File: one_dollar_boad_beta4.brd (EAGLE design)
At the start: 85.6 x 54 mm, 38 parts, among them IC1 ATTINY85, X1 USBPCB

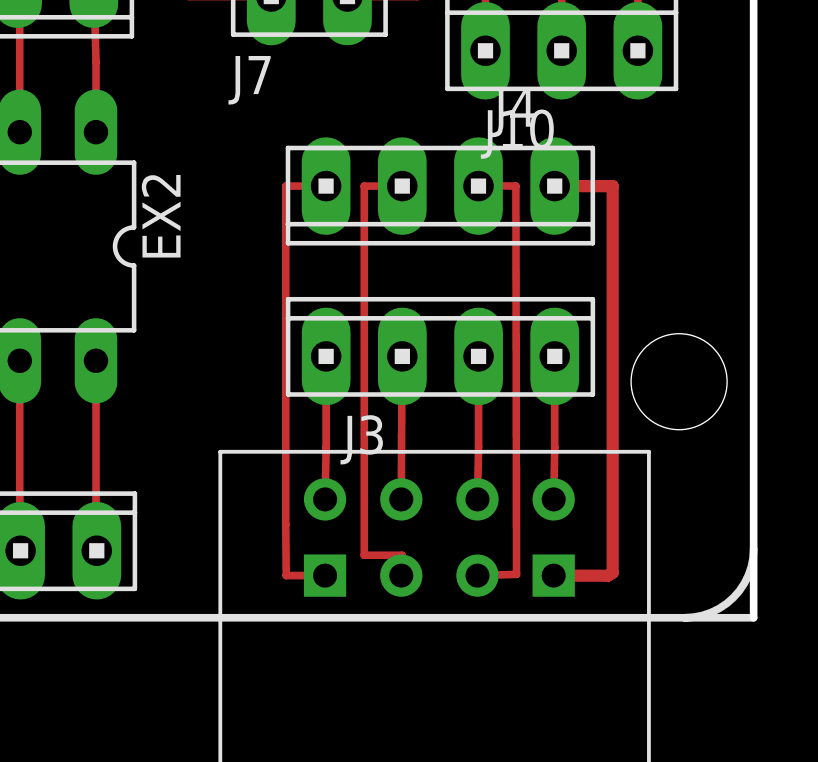
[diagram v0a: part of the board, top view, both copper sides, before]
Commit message: aumentada espessura das trilhas do ESP8266
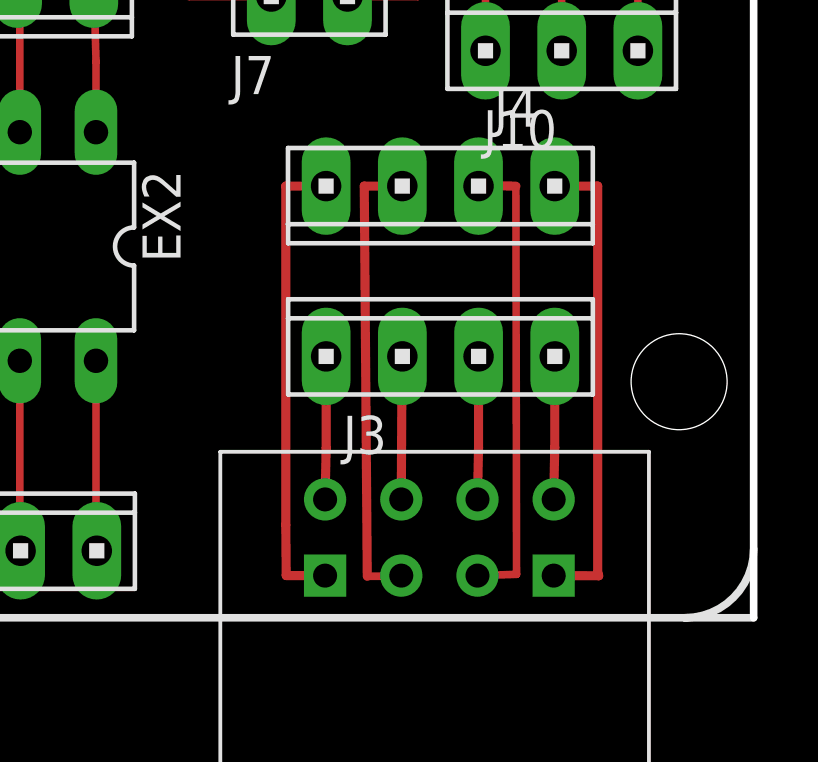
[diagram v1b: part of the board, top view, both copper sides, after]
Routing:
- net GND: track 108.6 -> 107.7 mm
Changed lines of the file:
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@@
 <text x="70.1" y="18.3" size="0.8128" layer="27">M2</text>
 <text x="73.6" y="52.5" size="0.8128" layer="27">M1</text>
-<text x="82.2" y="16.6" size="0.8128" layer="27">1</text>
+<text x="82.7" y="17.9" size="0.8128" layer="27">1</text>
 <text x="80.1" y="17.9" size="0.8128" layer="27">2</text>
 <text x="77.6" y="17.9" size="0.8128" layer="27">3</text>
@@
 <wire x1="0" y1="0" x2="85.6" y2="0" width="0.254" layer="21"/>
 <text x="70.3" y="4.4" size="0.8128" layer="27">5</text>
+<text x="82.7" y="22.4" size="0.8128" layer="27">1</text>
 </plain>
 <attributes>
@@
 <wire x1="69.3166" y1="32.9438" x2="69.3166" y2="27.4574" width="0.4064" layer="1"/>
 <contactref element="J4" pad="4"/>
-<wire x1="78.967" y1="14.3892" x2="80.9" y2="14.3892" width="0.4064" layer="1"/>
-<wire x1="80.9" y1="14.3892" x2="80.9" y2="1.5" width="0.4064" layer="1"/>
-<wire x1="80.9" y1="1.5" x2="80.7328" y2="1.4" width="0.4064" layer="1"/>
-<wire x1="80.7328" y1="1.4" x2="78.9328" y2="1.4053" width="0.4064" layer="1"/>
+<wire x1="78.967" y1="14.3892" x2="80.4" y2="14.3892" width="0.3048" layer="1"/>
+<wire x1="80.4" y1="14.3892" x2="80.4" y2="1.5" width="0.3048" layer="1"/>
+<wire x1="80.4" y1="1.5" x2="80.4328" y2="1.4" width="0.3048" layer="1"/>
+<wire x1="80.4328" y1="1.4" x2="78.9328" y2="1.4053" width="0.3048" layer="1"/>
 <wire x1="32.3088" y1="36.8808" x2="30" y2="36.8808" width="0.4064" layer="1"/>
 <wire x1="30" y1="36.8808" x2="30" y2="36.9" width="0.4064" layer="1"/>
@@
 <wire x1="76.3928" y1="1.4053" x2="77.6947" y2="1.4478" width="0.254" layer="1"/>
 <wire x1="77.6947" y1="1.4478" x2="77.6732" y2="14.3876" width="0.254" layer="1"/>
-<wire x1="77.6732" y1="14.3876" x2="76.4524" y2="14.413" width="0.254" layer="1"/>
+<wire x1="77.6732" y1="14.3876" x2="76.4524" y2="14.413" width="0.3048" layer="1"/>
 <wire x1="76.4524" y1="14.413" x2="76.427" y2="14.3892" width="0.254" layer="1"/>
 </signal>
@@
 <contactref element="U$8" pad="GPIO0"/>
 <contactref element="J4" pad="2"/>
-<wire x1="73.887" y1="14.3892" x2="72.6186" y2="14.3892" width="0.254" layer="1"/>
-<wire x1="72.6186" y1="14.3892" x2="72.6186" y2="2.0828" width="0.254" layer="1"/>
-<wire x1="72.6186" y1="2.0828" x2="73.8782" y2="2.0828" width="0.254" layer="1"/>
-<wire x1="73.8782" y1="2.0828" x2="73.8528" y2="1.4053" width="0.254" layer="1"/>
+<wire x1="73.887" y1="14.3892" x2="72.6186" y2="14.3892" width="0.3048" layer="1"/>
+<wire x1="72.6186" y1="14.3892" x2="72.7186" y2="1.3828" width="0.3048" layer="1"/>
+<wire x1="72.7186" y1="1.3828" x2="73.8782" y2="1.3828" width="0.254" layer="1"/>
+<wire x1="73.8782" y1="1.3828" x2="73.8528" y2="1.4053" width="0.254" layer="1"/>
 </signal>
 <signal name="N$31">
 <contactref element="U$8" pad="RX"/>
 <contactref element="J4" pad="1"/>
-<wire x1="71.347" y1="14.3892" x2="70.0024" y2="14.3892" width="0.254" layer="1"/>
-<wire x1="70.0024" y1="14.3892" x2="70.0024" y2="3.0988" width="0.254" layer="1"/>
-<wire x1="70.0024" y1="3.0988" x2="70.0174" y2="1.4066" width="0.254" layer="1"/>
-<wire x1="70.0174" y1="1.4066" x2="71.3128" y2="1.4053" width="0.254" layer="1"/>
+<wire x1="71.347" y1="14.3892" x2="70.0024" y2="14.3892" width="0.3048" layer="1"/>
+<wire x1="70.0024" y1="14.3892" x2="70.0024" y2="3.0988" width="0.3048" layer="1"/>
+<wire x1="70.0024" y1="3.0988" x2="70.0174" y2="1.4066" width="0.3048" layer="1"/>
+<wire x1="70.0174" y1="1.4066" x2="71.3128" y2="1.4053" width="0.3048" layer="1"/>
 </signal>
 <signal name="N$32">
 <contactref element="U$8" pad="TX"/>
 <contactref element="J3" pad="1"/>
-<wire x1="78.9686" y1="8.7122" x2="78.9686" y2="5.6779" width="0.254" layer="1"/>
-<wire x1="78.9686" y1="5.6779" x2="78.9328" y2="3.9453" width="0.254" layer="1"/>
+<wire x1="78.9686" y1="8.7122" x2="78.9686" y2="5.6779" width="0.3048" layer="1"/>
+<wire x1="78.9686" y1="5.6779" x2="78.9328" y2="3.9453" width="0.3048" layer="1"/>
 </signal>
 <signal name="N$33">
 <contactref element="U$8" pad="CH_PD"/>
 <contactref element="J3" pad="2"/>
-<wire x1="76.4286" y1="8.7122" x2="76.4286" y2="5.6779" width="0.254" layer="1"/>
-<wire x1="76.4286" y1="5.6779" x2="76.3928" y2="3.9453" width="0.254" layer="1"/>
+<wire x1="76.4286" y1="8.7122" x2="76.4286" y2="5.6779" width="0.3048" layer="1"/>
+<wire x1="76.4286" y1="5.6779" x2="76.3928" y2="3.9453" width="0.3048" layer="1"/>
 </signal>
 <signal name="N$34">
@@
 <contactref element="U$8" pad="RST"/>
 <wire x1="73.8886" y1="8.7122" x2="73.8782" y2="8.6868" width="0.254" layer="1"/>
-<wire x1="73.8782" y1="8.6868" x2="73.8528" y2="3.9453" width="0.254" layer="1"/>
+<wire x1="73.8782" y1="8.6868" x2="73.8528" y2="3.9453" width="0.3048" layer="1"/>
 </signal>
 <signal name="N$35">
 <contactref element="U$8" pad="VCC"/>
 <contactref element="J3" pad="4"/>
-<wire x1="71.3128" y1="3.9453" x2="71.3486" y2="5.6629" width="0.254" layer="1"/>
-<wire x1="71.3486" y1="5.6629" x2="71.3486" y2="8.7122" width="0.254" layer="1"/>
+<wire x1="71.3128" y1="3.9453" x2="71.3486" y2="5.6629" width="0.3048" layer="1"/>
+<wire x1="71.3486" y1="5.6629" x2="71.3486" y2="8.7122" width="0.3048" layer="1"/>
 </signal>
 <signal name="N$13">

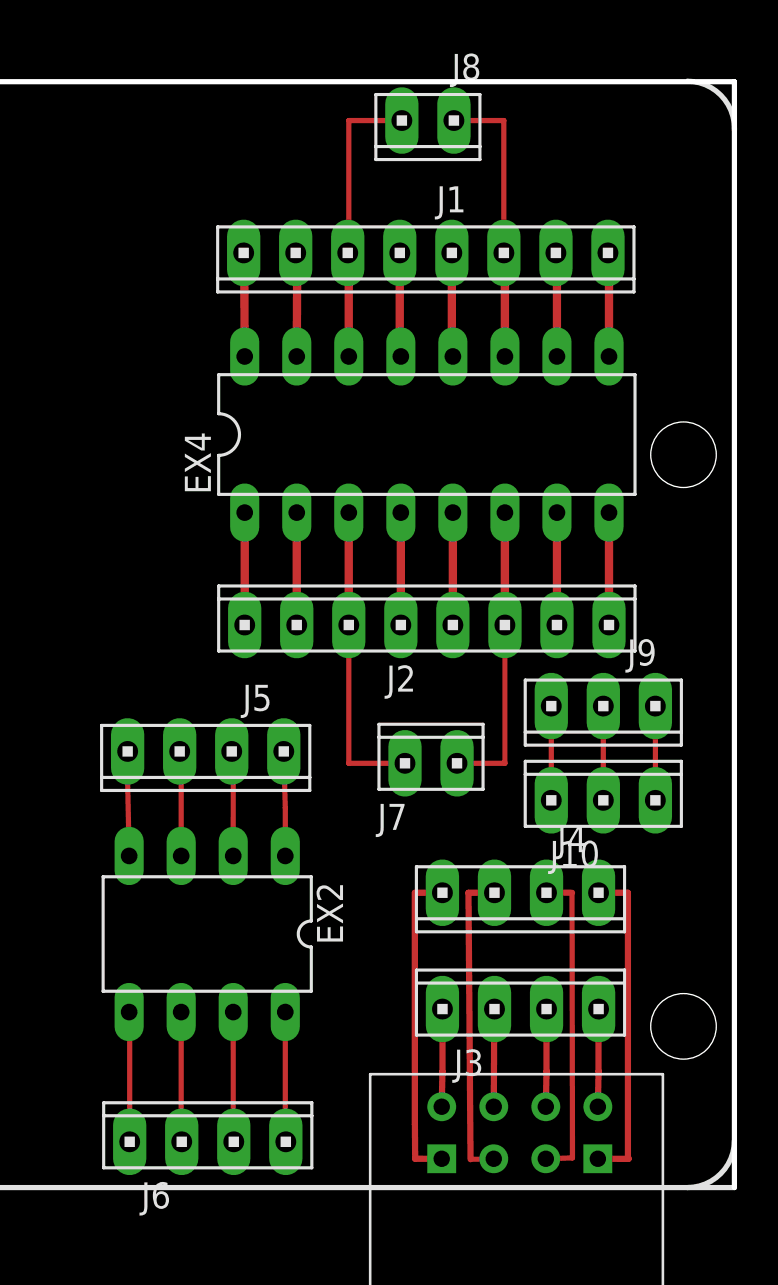
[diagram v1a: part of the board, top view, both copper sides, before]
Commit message: GND retirado
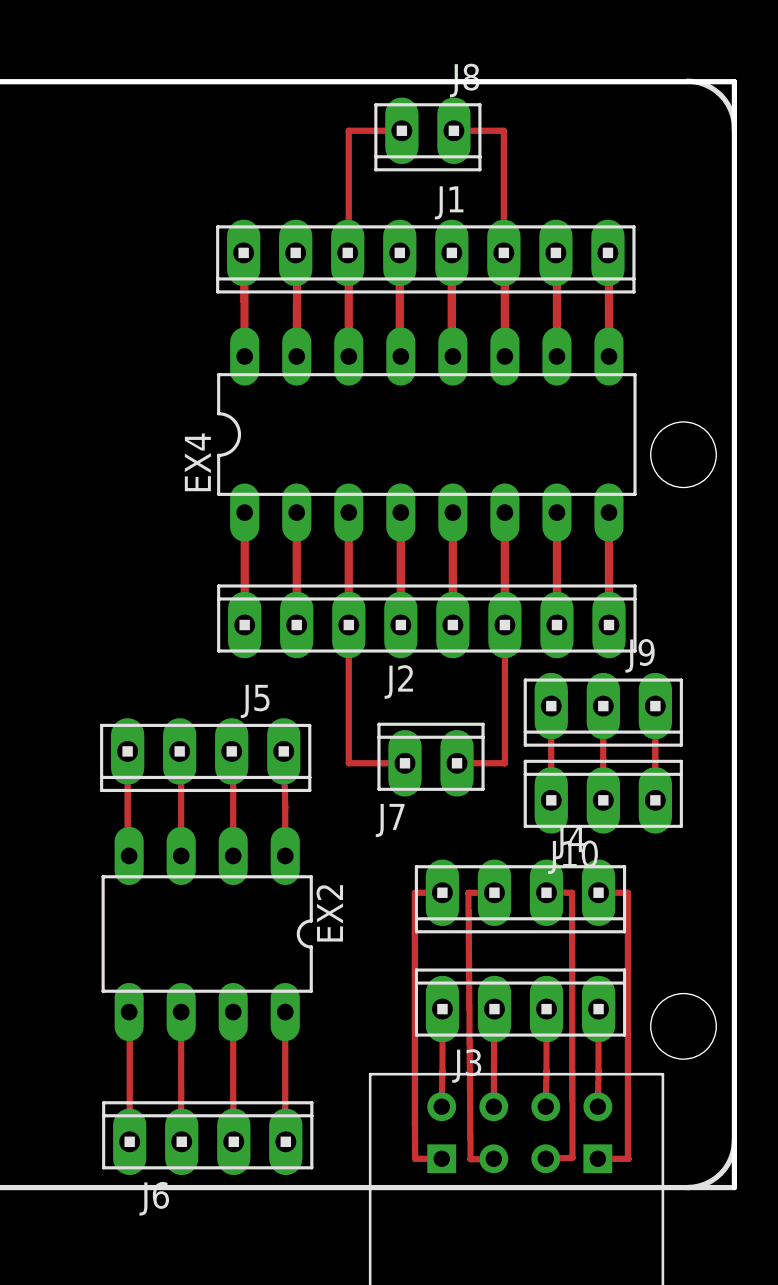
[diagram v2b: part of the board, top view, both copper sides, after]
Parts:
- moved J8 0.50 mm to (70.6, 51.6)
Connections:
- new net N$22: J4.4, U$8.GND
- new net N$49: EX4.5, J2.4
- new net N$50: EX4.4, J2.5
- new net N$51: EX4.12, J1.5
- new net N$52: EX4.13, J1.4
- new net N$53: EX2.4, J5.1
- net GND: no longer EX2.4, EX4.12, EX4.13, EX4.4, EX4.5, J1.4, J1.5, J2.4, J2.5, J4.4, U$8.GND
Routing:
- net GND: track 107.7 -> 65.4 mm
- net N$22: track 0.00 -> 15.9 mm
- net N$50: track 0.00 -> 5.49 mm
- net N$49: track 0.00 -> 5.49 mm
- net N$53: track 0.00 -> 5.13 mm
- net N$52: track 0.00 -> 5.11 mm
- net N$51: track 0.00 -> 5.11 mm
- net N$38: track 14.0 -> 13.5 mm
- net N$25: track 14.2 -> 13.7 mm

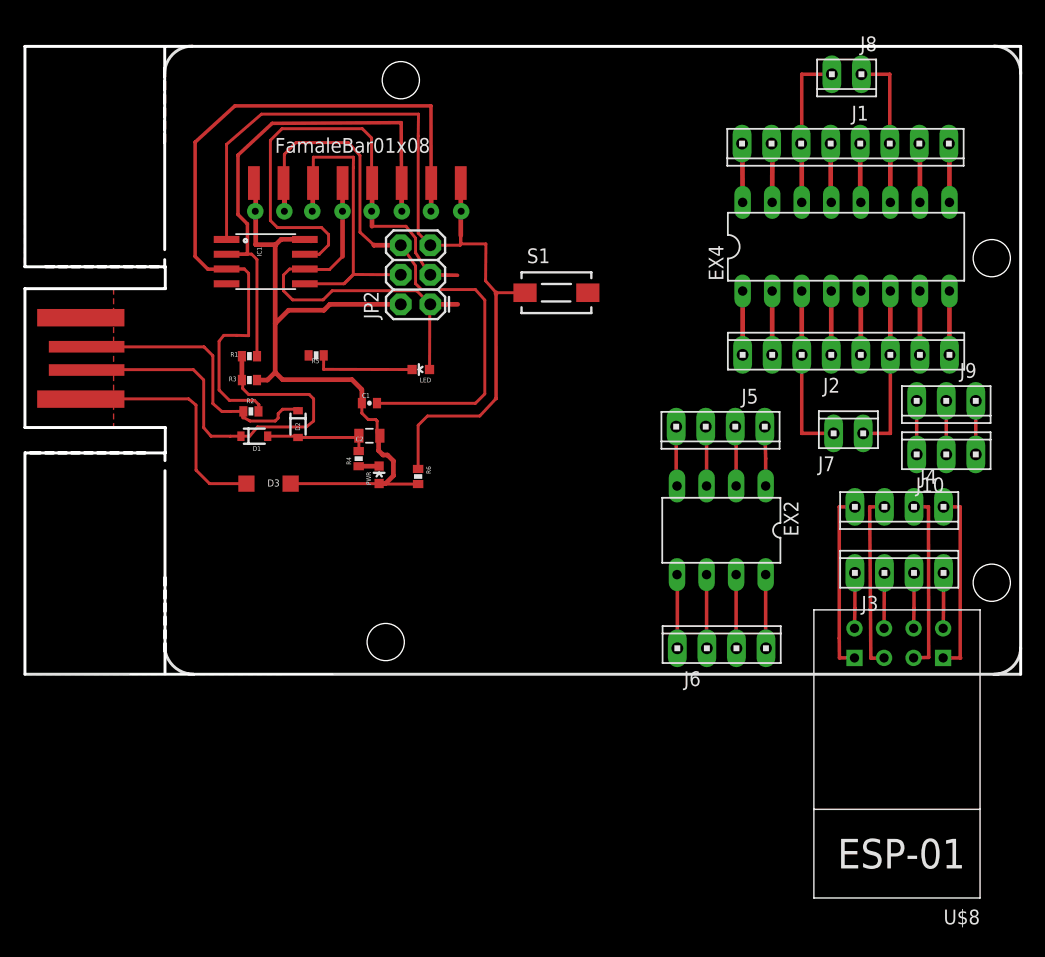
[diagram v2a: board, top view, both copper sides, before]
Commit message: Added files via upload
Adicionado alimentação externa
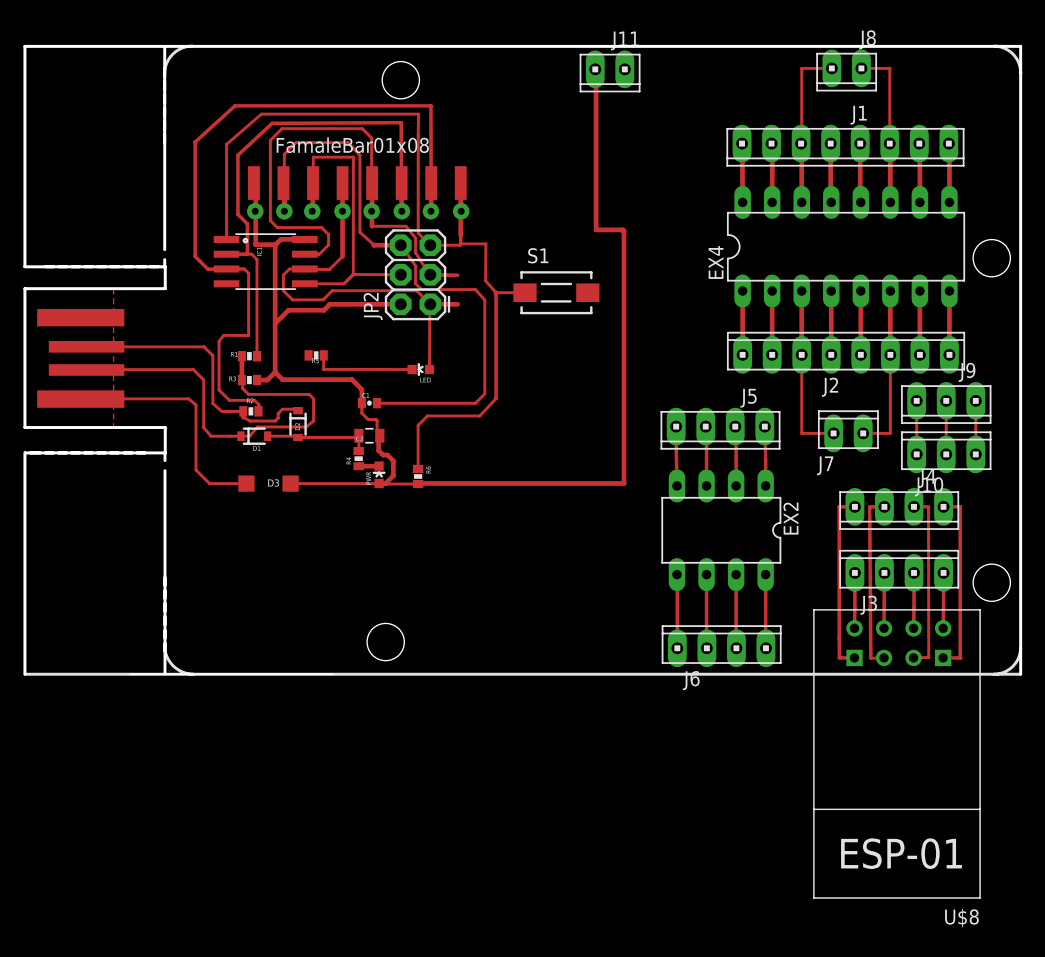
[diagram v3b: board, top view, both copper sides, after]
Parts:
- added J11: (no value), con-amp:10X02MTA
- moved J8 0.50 mm to (70.6, 52.1)
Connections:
- removed net N$22: J4.4, U$8.GND
- removed net N$49: EX4.5, J2.4
- removed net N$50: EX4.4, J2.5
- removed net N$51: EX4.12, J1.5
- removed net N$52: EX4.13, J1.4
- removed net N$53: EX2.4, J5.1
- net 5V: now also J11.1
- net GND: now also EX2.4, EX4.12, EX4.13, EX4.4, EX4.5, J1.4, J1.5, J11.2, J2.4, J2.5, J4.4, U$8.GND
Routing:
- net 5V: track 64.7 -> 120.5 mm
- net GND: track 65.4 -> 107.7 mm
- net N$22: track 15.9 -> 0.00 mm
- net N$50: track 5.49 -> 0.00 mm
- net N$49: track 5.49 -> 0.00 mm
- net N$53: track 5.13 -> 0.00 mm
- net N$52: track 5.11 -> 0.00 mm
- net N$51: track 5.11 -> 0.00 mm
- net N$38: track 13.5 -> 14.0 mm
- net N$25: track 13.7 -> 14.2 mm
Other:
- board text added: "POWER"
